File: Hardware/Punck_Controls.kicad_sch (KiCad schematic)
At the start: 36 parts, among them J1 Conn_01x12_Female, J10 Kick_In, J11 USB_B_Micro, J12 Tempo_Out, J13 Audio_Out_L, J14 Audio_Out_R, J15 Midi_In, J2 Conn_01x12_Female, J3 Conn_01x12_Female, J4 Conn_01x12_Female, J5 Snare_In, J6 CH_In, J7 OH_In, J8 SamplerA_In, J9 SamplerB_In

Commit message: More PCB tweaking
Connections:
- net AUDIO_OUT_L: now also J4.10 (Pin_10); no longer J4.9 (Pin_9)
- net CH_IN: now also J2.7 (Pin_7); no longer J2.6 (Pin_6)
- net GND: now also J2.1 (Pin_1), J4.8 (Pin_8), J4.9 (Pin_9); no longer J4.1 (Pin_1)
- net HH_BTN: now also J2.5 (Pin_5); no longer J2.4 (Pin_4)
- net HH_LED: now also J4.6 (Pin_6); no longer J4.7 (Pin_7)
- net HIHAT_VOL_POT: now also J2.2 (Pin_2); no longer J2.1 (Pin_1)
- net KI_LED: now also J4.4 (Pin_4); no longer J4.5 (Pin_5)
- net MIDI_LEARN: now also J3.8 (Pin_8); no longer J2.10 (Pin_10)
- net OH_IN: now also J2.8 (Pin_8); no longer J2.7 (Pin_7)
- net SAMPLER_A_IN: now also J2.9 (Pin_9); no longer J2.8 (Pin_8)
- net SAMPLER_A_VOL_POT: now also J2.3 (Pin_3); no longer J2.2 (Pin_2)
- net SAMPLER_B_IN: now also J2.10 (Pin_10); no longer J2.9 (Pin_9)
- net SAMPLER_B_VOL_POT: now also J2.4 (Pin_4); no longer J2.3 (Pin_3)
- net SEQ_SELECT: now also J4.7 (Pin_7); no longer J2.11 (Pin_11)
- net SN_LED: now also J4.5 (Pin_5); no longer J4.6 (Pin_6)
- net TEMPO_OUT: now also J2.11 (Pin_11); no longer J4.10 (Pin_10)
- net TEMPO_POT: now also J2.6 (Pin_6); no longer J2.5 (Pin_5)
- net USB_DM: now also J4.2 (Pin_2); no longer J4.3 (Pin_3)
- net USB_DP: now also J4.1 (Pin_1); no longer J4.2 (Pin_2)
- net USB_VBUS: now also J4.3 (Pin_3); no longer J4.4 (Pin_4)
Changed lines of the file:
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@@
   (junction (at 135.89 133.35) (diameter 0) (color 0 0 0 0)
+  )
+  (junction (at 256.54 152.4) (diameter 0) (color 0 0 0 0)
   )
   (junction (at 77.47 133.35) (diameter 0) (color 0 0 0 0)
@@
     (stroke (width 0) (type default) (color 0 0 0 0))
   )
+  (wire (pts (xy 252.73 151.13) (xy 256.54 151.13))
+    (stroke (width 0) (type default) (color 0 0 0 0))
+  )
   (wire (pts (xy 69.85 72.39) (xy 69.85 74.93))
     (stroke (width 0) (type default) (color 0 0 0 0))
@@
     (stroke (width 0) (type default) (color 0 0 0 0))
   )
+  (wire (pts (xy 256.54 153.67) (xy 256.54 152.4))
+    (stroke (width 0) (type default) (color 0 0 0 0))
+  )
   (wire (pts (xy 133.35 128.27) (xy 135.89 128.27))
     (stroke (width 0) (type default) (color 0 0 0 0))
@@
     (stroke (width 0) (type default) (color 0 0 0 0))
   )
+  (wire (pts (xy 252.73 153.67) (xy 256.54 153.67))
+    (stroke (width 0) (type default) (color 0 0 0 0))
+  )
   (wire (pts (xy 161.29 50.8) (xy 163.83 50.8))
     (stroke (width 0) (type default) (color 0 0 0 0))
@@
   )
   (wire (pts (xy 43.18 191.77) (xy 45.72 191.77))
+    (stroke (width 0) (type default) (color 0 0 0 0))
+  )
+  (wire (pts (xy 256.54 152.4) (xy 256.54 151.13))
     (stroke (width 0) (type default) (color 0 0 0 0))
   )
@@
     (effects (font (size 1.27 1.27)) (justify left bottom))
   )
-  (label "CH_IN" (at 252.73 71.12 0)
+  (label "CH_IN" (at 252.73 73.66 0)
     (effects (font (size 1.27 1.27)) (justify left bottom))
   )
@@
     (effects (font (size 1.27 1.27)) (justify left bottom))
   )
-  (label "KI_LED" (at 252.73 143.51 0)
-    (effects (font (size 1.27 1.27)) (justify left bottom))
-  )
-  (label "SAMPLER_A_VOL_POT" (at 252.73 60.96 0)
+  (label "KI_LED" (at 252.73 140.97 0)
+    (effects (font (size 1.27 1.27)) (justify left bottom))
+  )
+  (label "SAMPLER_A_VOL_POT" (at 252.73 63.5 0)
     (effects (font (size 1.27 1.27)) (justify left bottom))
   )
@@
     (effects (font (size 1.27 1.27)) (justify left bottom))
   )
-  (label "USB_DM" (at 252.73 138.43 0)
+  (label "USB_DM" (at 252.73 135.89 0)
     (effects (font (size 1.27 1.27)) (justify left bottom))
   )
@@
     (effects (font (size 1.27 1.27)) (justify left bottom))
   )
-  (label "USB_VBUS" (at 252.73 140.97 0)
+  (label "USB_VBUS" (at 252.73 138.43 0)
     (effects (font (size 1.27 1.27)) (justify left bottom))
   )
@@
     (effects (font (size 1.27 1.27)) (justify left bottom))
   )
-  (label "SEQ_SELECT" (at 252.73 83.82 0)
+  (label "SEQ_SELECT" (at 252.73 148.59 0)
     (effects (font (size 1.27 1.27)) (justify left bottom))
   )
@@
     (effects (font (size 1.27 1.27)) (justify right bottom))
   )
-  (label "TEMPO_OUT" (at 252.73 156.21 0)
+  (label "TEMPO_OUT" (at 252.73 83.82 0)
     (effects (font (size 1.27 1.27)) (justify left bottom))
   )
@@
     (effects (font (size 1.27 1.27)) (justify left bottom))
   )
-  (label "HH_BTN" (at 252.73 66.04 0)
-    (effects (font (size 1.27 1.27)) (justify left bottom))
-  )
-  (label "HIHAT_VOL_POT" (at 252.73 58.42 0)
-    (effects (font (size 1.27 1.27)) (justify left bottom))
-  )
-  (label "SN_LED" (at 252.73 146.05 0)
-    (effects (font (size 1.27 1.27)) (justify left bottom))
-  )
-  (label "HH_LED" (at 252.73 148.59 0)
-    (effects (font (size 1.27 1.27)) (justify left bottom))
-  )
-  (label "USB_DP" (at 252.73 135.89 0)
+  (label "HH_BTN" (at 252.73 68.58 0)
+    (effects (font (size 1.27 1.27)) (justify left bottom))
+  )
+  (label "HIHAT_VOL_POT" (at 252.73 60.96 0)
+    (effects (font (size 1.27 1.27)) (justify left bottom))
+  )
+  (label "SN_LED" (at 252.73 143.51 0)
+    (effects (font (size 1.27 1.27)) (justify left bottom))
+  )
+  (label "HH_LED" (at 252.73 146.05 0)
+    (effects (font (size 1.27 1.27)) (justify left bottom))
+  )
+  (label "USB_DP" (at 252.73 133.35 0)
     (effects (font (size 1.27 1.27)) (justify left bottom))
   )
@@
     (effects (font (size 1.27 1.27)) (justify right bottom))
   )
-  (label "MIDI_LEARN" (at 252.73 81.28 0)
+  (label "MIDI_LEARN" (at 252.73 113.03 0)
     (effects (font (size 1.27 1.27)) (justify left bottom))
   )
@@
     (effects (font (size 1.27 1.27)) (justify right bottom))
   )
-  (label "SAMPLER_A_IN" (at 252.73 76.2 0)
+  (label "SAMPLER_A_IN" (at 252.73 78.74 0)
     (effects (font (size 1.27 1.27)) (justify left bottom))
   )
@@
     (effects (font (size 1.27 1.27)) (justify left bottom))
   )
-  (label "SAMPLER_B_IN" (at 252.73 78.74 0)
+  (label "SAMPLER_B_IN" (at 252.73 81.28 0)
     (effects (font (size 1.27 1.27)) (justify left bottom))
   )
@@
     (effects (font (size 1.27 1.27)) (justify left bottom))
   )
-  (label "OH_IN" (at 252.73 73.66 0)
+  (label "OH_IN" (at 252.73 76.2 0)
     (effects (font (size 1.27 1.27)) (justify left bottom))
   )
@@
     (effects (font (size 1.27 1.27)) (justify left bottom))
   )
-  (label "AUDIO_OUT_L" (at 252.73 153.67 0)
+  (label "AUDIO_OUT_L" (at 252.73 156.21 0)
     (effects (font (size 1.27 1.27)) (justify left bottom))
   )
@@
     (effects (font (size 1.27 1.27)) (justify left bottom))
   )
-  (label "SAMPLER_B_VOL_POT" (at 252.73 63.5 0)
+  (label "SAMPLER_B_VOL_POT" (at 252.73 66.04 0)
     (effects (font (size 1.27 1.27)) (justify left bottom))
   )
@@
     (effects (font (size 1.27 1.27)) (justify left bottom))
   )
-  (label "TEMPO_POT" (at 252.73 68.58 0)
+  (label "TEMPO_POT" (at 252.73 71.12 0)
     (effects (font (size 1.27 1.27)) (justify left bottom))
   )
@@
     (pin "1")
   )
-  (symbol (lib_id "power:GND") (at 252.73 133.35 90) (unit 1)
-    (in_bom yes) (on_board yes)
-    (property "Reference" "#PWR0101" (id 0) (at 259.08 133.35 0)
-      (effects (font (size 1.27 1.27)) hide)
-    )
-    (property "Value" "GND" (id 1) (at 257.81 132.08 90))
-    (property "Footprint" "" (id 2) (at 252.73 133.35 0)
-      (effects (font (size 1.27 1.27)) hide)
-    )
-    (property "Datasheet" "" (id 3) (at 252.73 133.35 0)
+  (symbol (lib_id "power:GND") (at 256.54 152.4 90) (unit 1)
+    (in_bom yes) (on_board yes)
+    (property "Reference" "#PWR0101" (id 0) (at 262.89 152.4 0)
+      (effects (font (size 1.27 1.27)) hide)
+    )
+    (property "Value" "GND" (id 1) (at 261.62 151.13 90))
+    (property "Footprint" "" (id 2) (at 256.54 152.4 0)
+      (effects (font (size 1.27 1.27)) hide)
+    )
+    (property "Datasheet" "" (id 3) (at 256.54 152.4 0)
       (effects (font (size 1.27 1.27)) hide)
     )
@@
     (pin "3")
   )
+  (symbol (lib_id "power:GND") (at 252.73 58.42 90) (unit 1)
+    (in_bom yes) (on_board yes)
+    (property "Reference" "#PWR0107" (id 0) (at 259.08 58.42 0)
+      (effects (font (size 1.27 1.27)) hide)
+    )
+    (property "Value" "GND" (id 1) (at 257.81 57.15 90))
+    (property "Footprint" "" (id 2) (at 252.73 58.42 0)
+      (effects (font (size 1.27 1.27)) hide)
+    )
+    (property "Datasheet" "" (id 3) (at 252.73 58.42 0)
+      (effects (font (size 1.27 1.27)) hide)
+    )
+    (pin "1")
+  )
   (symbol (lib_id "power:GND") (at 252.73 20.32 90) (unit 1)
     (in_bom yes) (on_board yes)
@@
       (reference "#PWR0106") (unit 1) (value "+3.3VA") (footprint "")
     )
+    (path "/c269bd85-a27f-4da9-a399-1bdfcd17cddb"
+      (reference "#PWR0107") (unit 1) (value "GND") (footprint "")
+    )
     (path "/990184b4-4444-4c3c-9341-d5ee4a989dd2"

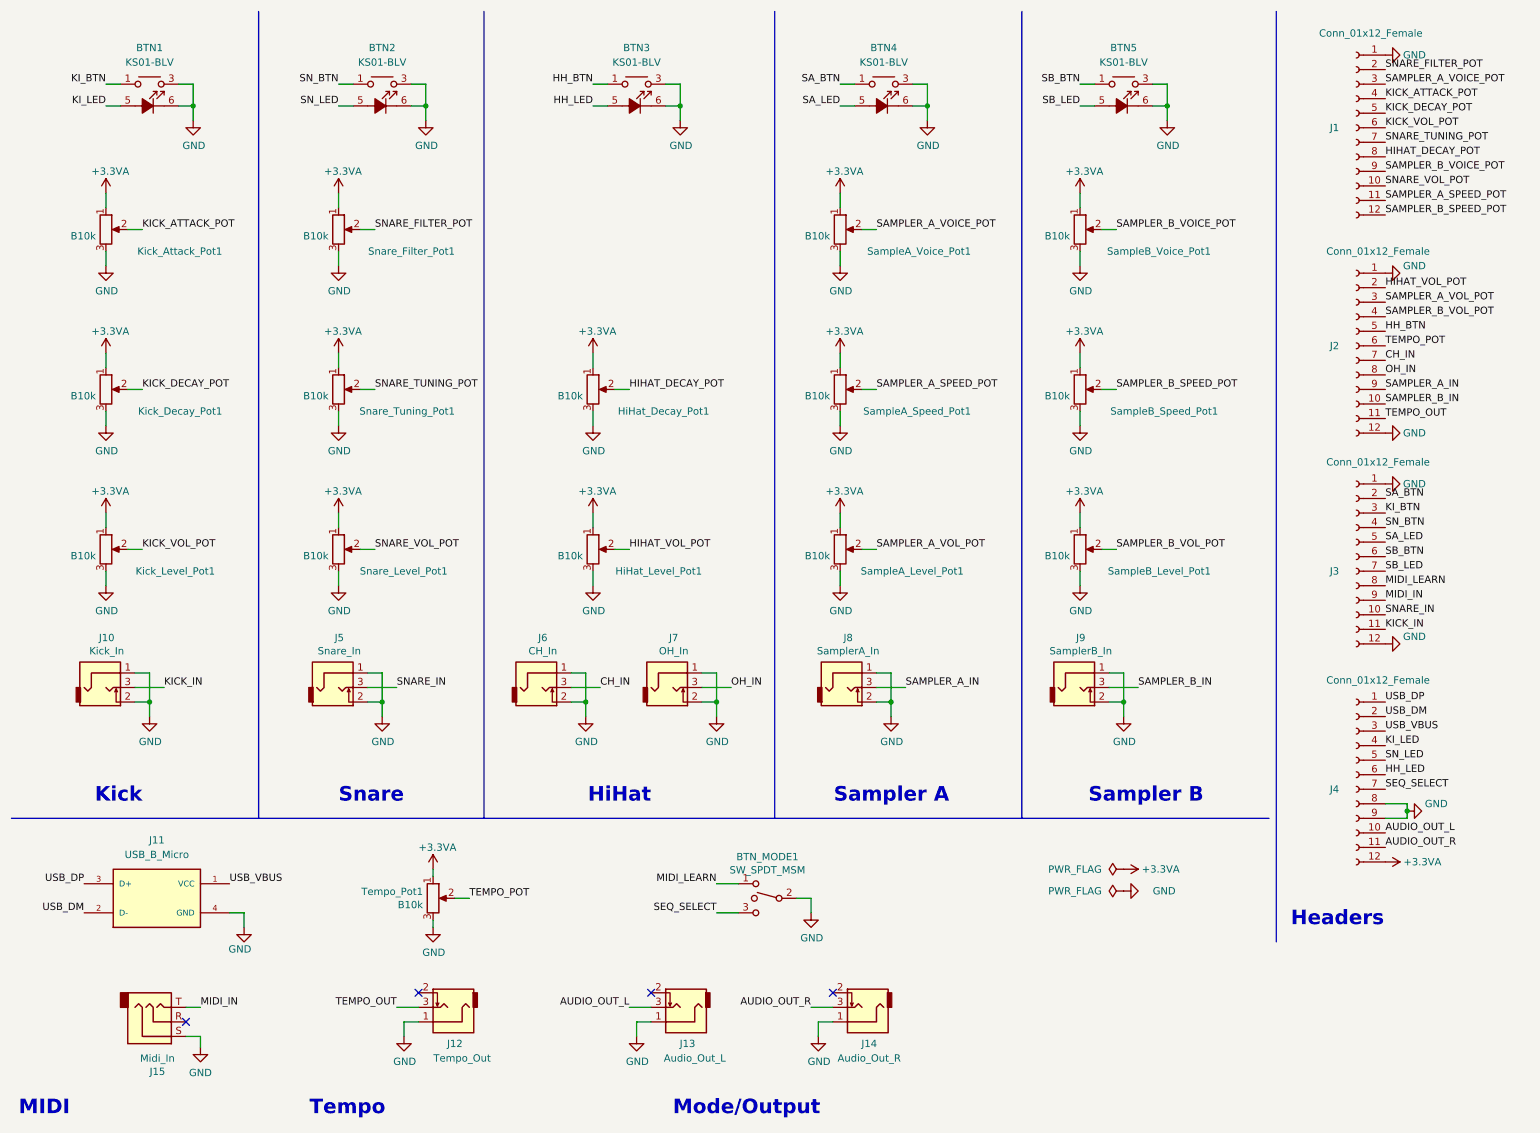
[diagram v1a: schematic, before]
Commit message: More PCB tweaks; rejigged bottom row of controls
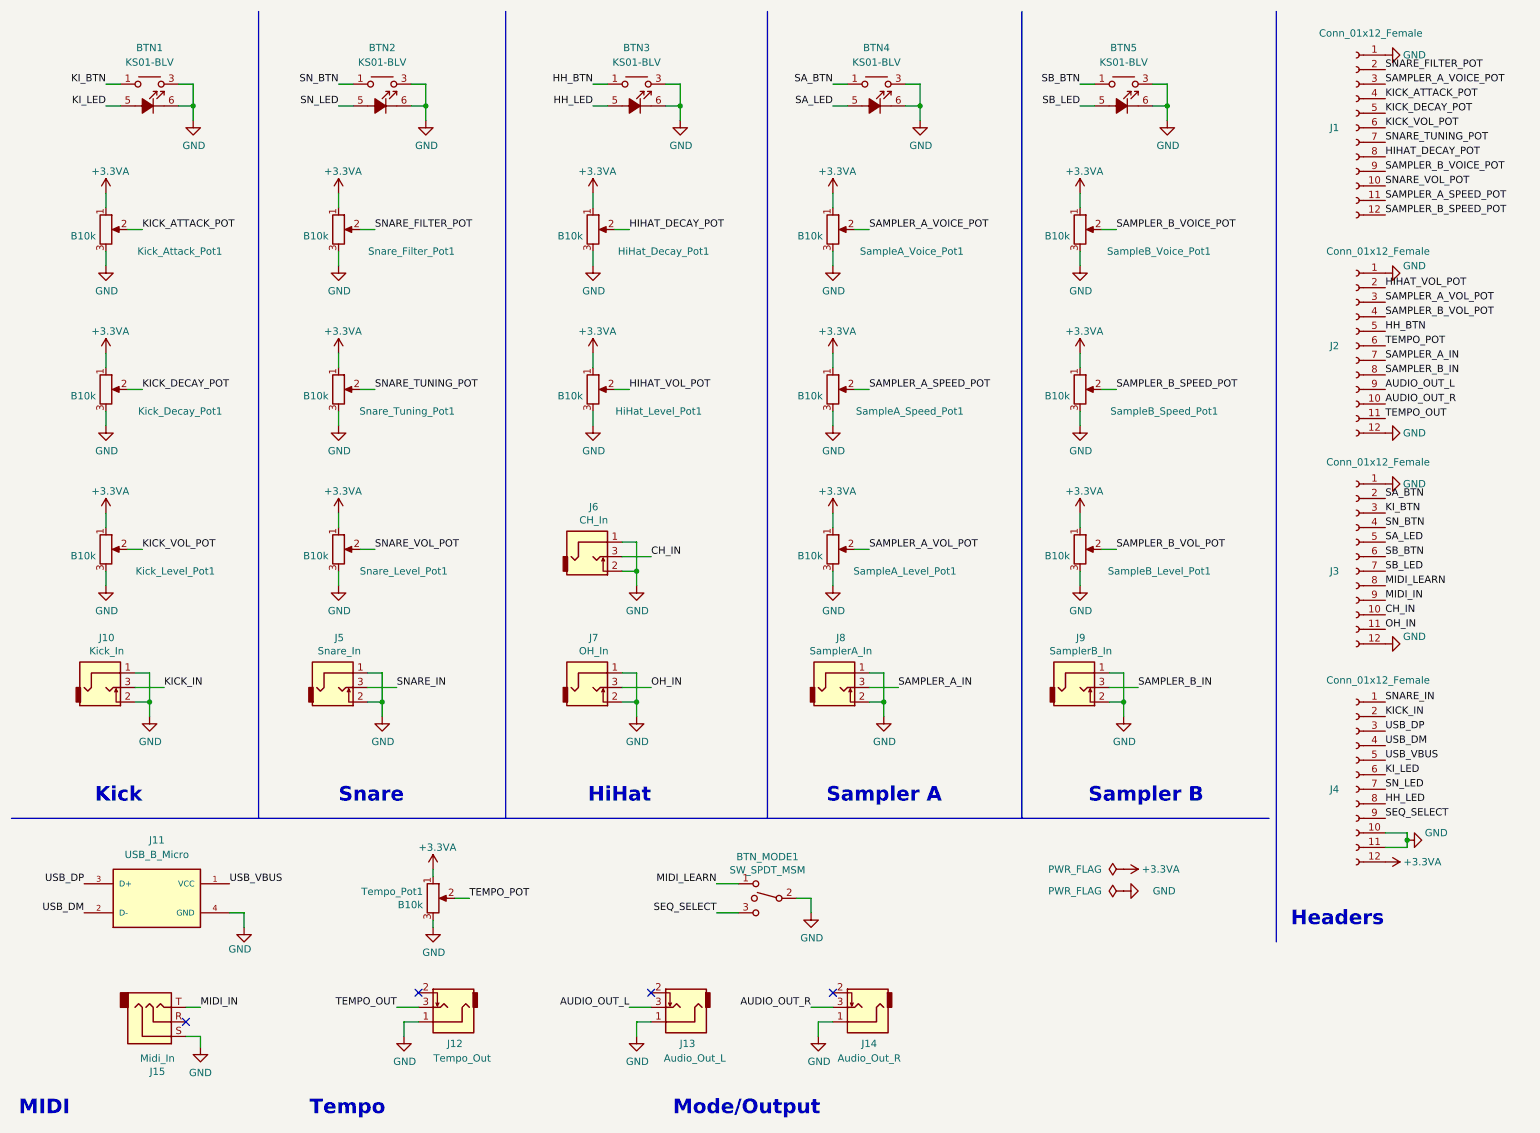
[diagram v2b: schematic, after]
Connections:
- net AUDIO_OUT_L: now also J2.9 (Pin_9); no longer J4.10 (Pin_10)
- net AUDIO_OUT_R: now also J2.10 (Pin_10); no longer J4.11 (Pin_11)
- net CH_IN: now also J3.10 (Pin_10); no longer J2.7 (Pin_7)
- net GND: now also J4.10 (Pin_10), J4.11 (Pin_11); no longer J4.8 (Pin_8), J4.9 (Pin_9)
- net HH_LED: now also J4.8 (Pin_8); no longer J4.6 (Pin_6)
- net KICK_IN: now also J4.2 (Pin_2); no longer J3.11 (Pin_11)
- net KI_LED: now also J4.6 (Pin_6); no longer J4.4 (Pin_4)
- net OH_IN: now also J3.11 (Pin_11); no longer J2.8 (Pin_8)
- net SAMPLER_A_IN: now also J2.7 (Pin_7); no longer J2.9 (Pin_9)
- net SAMPLER_B_IN: now also J2.8 (Pin_8); no longer J2.10 (Pin_10)
- net SEQ_SELECT: now also J4.9 (Pin_9); no longer J4.7 (Pin_7)
- net SNARE_IN: now also J4.1 (Pin_1); no longer J3.10 (Pin_10)
- net SN_LED: now also J4.7 (Pin_7); no longer J4.5 (Pin_5)
- net USB_DM: now also J4.4 (Pin_4); no longer J4.2 (Pin_2)
- net USB_DP: now also J4.3 (Pin_3); no longer J4.1 (Pin_1)
- net USB_VBUS: now also J4.5 (Pin_5); no longer J4.3 (Pin_3)
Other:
- moved on the sheet: BTN4, HiHat_Decay_Pot1, HiHat_Level_Pot1, J6, J7, J8, SampleA_Level_Pot1, SampleA_Speed_Pot1, SampleA_Voice_Pot1

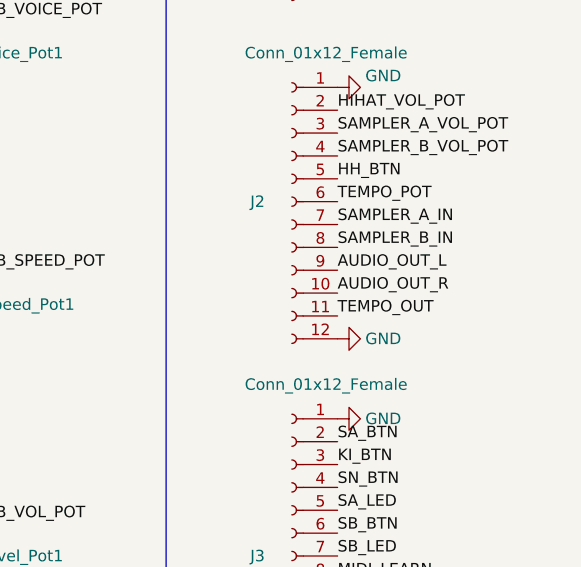
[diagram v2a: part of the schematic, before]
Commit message: Added test code to use PWM control on voice LEDs
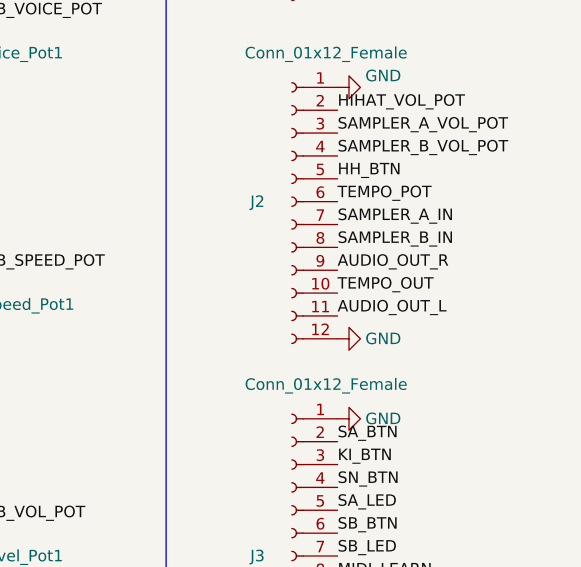
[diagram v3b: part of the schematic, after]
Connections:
- net AUDIO_OUT_L: now also J2.11 (Pin_11); no longer J2.9 (Pin_9)
- net AUDIO_OUT_R: now also J2.9 (Pin_9); no longer J2.10 (Pin_10)
- net TEMPO_OUT: now also J2.10 (Pin_10); no longer J2.11 (Pin_11)
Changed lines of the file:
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@@
     (effects (font (size 1.27 1.27)) (justify right bottom))
   )
-  (label "AUDIO_OUT_R" (at 252.73 81.28 0)
+  (label "AUDIO_OUT_R" (at 252.73 78.74 0)
     (effects (font (size 1.27 1.27)) (justify left bottom))
   )
@@
     (effects (font (size 1.27 1.27)) (justify right bottom))
   )
-  (label "TEMPO_OUT" (at 252.73 83.82 0)
+  (label "TEMPO_OUT" (at 252.73 81.28 0)
     (effects (font (size 1.27 1.27)) (justify left bottom))
   )
@@
     (effects (font (size 1.27 1.27)) (justify left bottom))
   )
-  (label "AUDIO_OUT_L" (at 252.73 78.74 0)
+  (label "AUDIO_OUT_L" (at 252.73 83.82 0)
     (effects (font (size 1.27 1.27)) (justify left bottom))
   )
